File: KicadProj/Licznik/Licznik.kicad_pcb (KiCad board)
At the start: 2 copper layers, 15 parts, among them J1 RTC Module, J2 7Seg-Display, J3 GND_IN, J4 POWER_IN, J5 +, J7 +, J8 -, J9 +, U1 ATmega328P-PU, Y1 Crystal

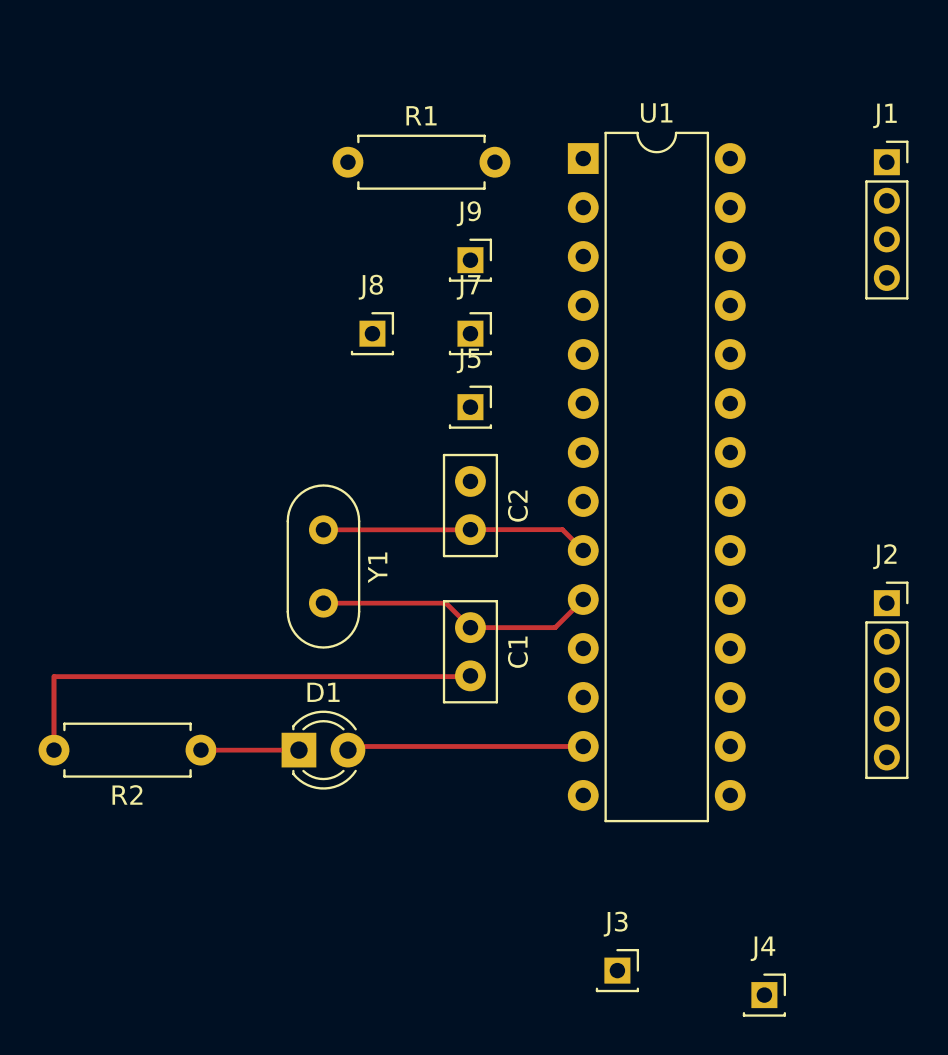
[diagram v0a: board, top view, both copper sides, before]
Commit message: created PCB board
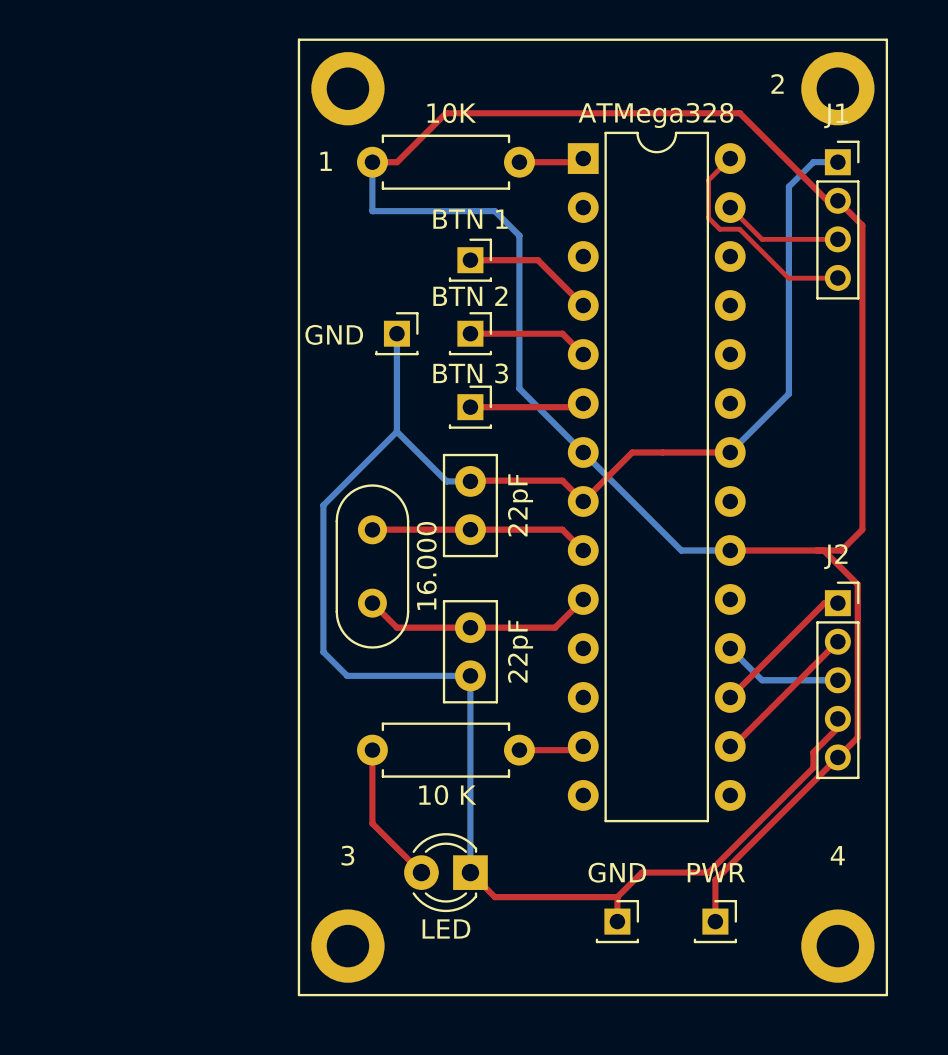
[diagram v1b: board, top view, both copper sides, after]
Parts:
- added 1: 1, MountingHole:MountingHole_2.2mm_M2_DIN965_Pad, F.Cu at (92.7, 76.2)
- added 2: 1, MountingHole:MountingHole_2.2mm_M2_DIN965_Pad, F.Cu at (118.1, 76.2)
- added 3: 1, MountingHole:MountingHole_2.2mm_M2_DIN965_Pad, F.Cu at (92.7, 120.7)
- added 4: 1, MountingHole:MountingHole_2.2mm_M2_DIN965_Pad, F.Cu at (118.1, 120.7)
- 10 K: renamed from R2
- BTN 1: renamed from J9
- BTN 2: renamed from J7
- BTN 3: renamed from J5
- J1: value RTC Module -> rtc
- J2: value 7Seg-Display -> 7seg
- moved 10 K 16.5 mm to (101.6, 110.5)
- moved LED 10.9 mm to (99.1, 116.8), turned to 180 degrees
- moved 10K 8.89 mm to (101.6, 80.0), turned to 180 degrees
- moved PWR 4.58 mm to (111.8, 119.4)
- moved 16.000 2.54 mm to (94.0, 99.1)
- moved GND 2.54 mm to (106.7, 119.4)
- moved J1 2.54 mm to (118.1, 80.0)
- moved J2 2.54 mm to (118.1, 102.9)
- moved GND 1.27 mm to (95.2, 88.9)
- renumbered R1 to 10K, Y1 to 16.000, C2 to 22pF, C1 to 22pF, U1 to ATMega328, J8 to GND, J3 to GND, D1 to LED, J4 to PWR
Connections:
- 10 K pad 1: Net-(D1-Pad1) -> Net-(R2-Pad1)
- 10 K pad 2: GND -> Net-(D1-Pad2)
- ATMega328 pad 13: Net-(D1-Pad2) -> Net-(R2-Pad1)
- LED pad 1: Net-(D1-Pad1) -> GND
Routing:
- net +5V: track 0.00 -> 108.3 mm
- net GND: track 25.4 -> 99.9 mm
- net Net-(J1-Pad4): track 0.00 -> 11.6 mm
- net Net-(J2-Pad2): track 0.00 -> 7.83 mm
- net Net-(J2-Pad1): track 0.00 -> 7.61 mm
- net Net-(J9-Pad1): track 0.00 -> 6.82 mm
- net Net-(J7-Pad1): track 0.00 -> 6.30 mm
- net Net-(J2-Pad3): track 0.00 -> 6.26 mm
- net Net-(J1-Pad3): track 0.00 -> 6.26 mm
- net Net-(J5-Pad1): track 0.00 -> 5.93 mm
- net Net-(D1-Pad1): track 5.08 -> 0.00 mm
- net Net-(D1-Pad2): track 12.3 -> 7.40 mm
- net Net-(R2-Pad1): track 0.00 -> 3.66 mm
- net Net-(R1-Pad1): track 0.00 -> 3.39 mm
- net Net-(C1-Pad1): track 14.9 -> 12.3 mm
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
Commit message: update schematics
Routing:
- added copper zone on B.Cu, net GND
- added copper zone on F.Cu, net GND
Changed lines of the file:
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@@
       (drillshape 0)
       (scaleselection 1)
-      (outputdirectory "../../../../KiCadProj/Render/"))
+      (outputdirectory "Output/"))
   )
   (net 0 "")
@@
   (segment (start 104.72 110.49) (end 104.91 110.3) (width 0.32) (layer F.Cu) (net 27))
   (segment (start 101.6 110.49) (end 104.72 110.49) (width 0.32) (layer F.Cu) (net 27))
+  (zone (net 1) (net_name GND) (layer F.Cu) (hatch edge 0.508)
+    (connect_pads (clearance 0.508))
+    (min_thickness 0.254)
+    (fill yes (arc_segments 32) (thermal_gap 0.508) (thermal_bridge_width 0.508))
+    (polygon
+      (pts
+        (xy 120.65 123.19) (xy 90.17 123.19) (xy 90.17 73.66) (xy 120.65 73.66)
+      )
+    )
+  )
+  (zone (net 1) (net_name GND) (layer B.Cu) (hatch edge 0.508)
+    (connect_pads (clearance 0.508))
+    (min_thickness 0.254)
+    (fill yes (arc_segments 32) (thermal_gap 0.508) (thermal_bridge_width 0.508))
+    (polygon
+      (pts
+        (xy 120.65 123.19) (xy 90.17 123.19) (xy 90.17 73.66) (xy 120.65 73.66)
+      )
+    )
+  )
 )
